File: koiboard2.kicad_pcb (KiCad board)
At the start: 2 copper layers, 227 x 75.4 mm, 137 parts, among them J1 Conn_01x04, J2 USB_C_Receptacle_USB2.0_16P, J3 Conn_01x05, SW1 choc_v1_SW_HS, SW10 choc_v1_SW_HS, SW11 choc_v1_SW_HS, SW12 choc_v1_SW_HS, SW13 choc_v1_SW_HS, SW14 choc_v1_SW_HS, SW15 choc_v1_SW_HS, SW16 choc_v1_SW_HS, SW17 choc_v1_SW_HS, SW18 choc_v1_SW_HS, SW19 choc_v1_SW_HS, SW2 choc_v1_SW_HS, SW20 choc_v1_SW_HS, SW21 choc_v1_SW_HS, SW22 choc_v1_SW_HS, SW23 choc_v1_SW_HS, SW24 choc_v1_SW_HS, SW25 choc_v1_SW_HS, SW26 choc_v1_SW_HS, SW27 choc_v1_SW_HS, SW28 choc_v1_SW_HS, SW29 choc_v1_SW_HS, SW3 choc_v1_SW_HS, SW30 choc_v1_SW_HS, SW31 choc_v1_SW_HS, SW32 choc_v1_SW_HS, SW33 choc_v1_SW_HS, SW34 choc_v1_SW_HS, SW35 choc_v1_SW_HS, SW36 choc_v1_SW_HS, SW37 choc_v1_SW_HS, SW38 choc_v1_SW_HS, SW39 choc_v1_SW_HS, SW4 choc_v1_SW_HS, SW40 choc_v1_SW_HS, SW41 choc_v1_SW_HS, SW42 choc_v1_SW_HS, SW43 choc_v1_SW_HS, SW44 choc_v1_SW_HS, SW45 choc_v1_SW_HS, SW46 choc_v1_SW_HS, SW47 choc_v1_SW_HS, SW5 choc_v1_SW_HS, SW6 choc_v1_SW_HS, SW7 choc_v1_SW_HS, SW8 choc_v1_SW_HS, SW9 choc_v1_SW_HS, U1 XC6206PxxxMR, U2 SRV05-4, U3 RP2040, U4 W25Q128JVS, Y1 Crystal_GND24

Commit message: silkscreen update
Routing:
- net GND: vias 104 -> 106
- net (no net): vias 0 -> 2
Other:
- board text added: "こいぼーど"

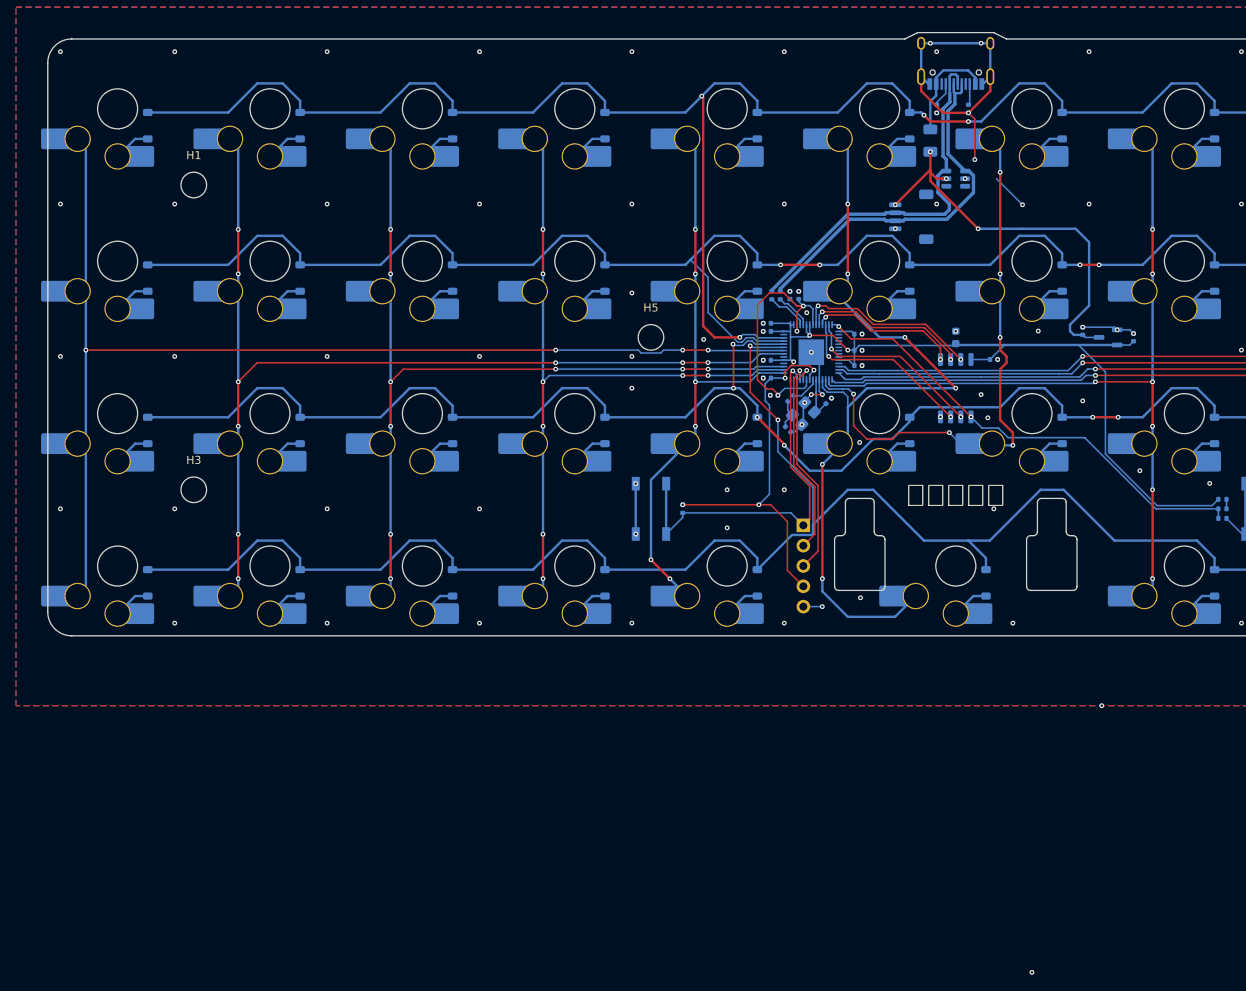
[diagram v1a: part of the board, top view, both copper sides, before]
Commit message: update
new 3d files, stab removed, logo moved, 2x1u <-> 2u support, cleanup, pcb dxf, ect...
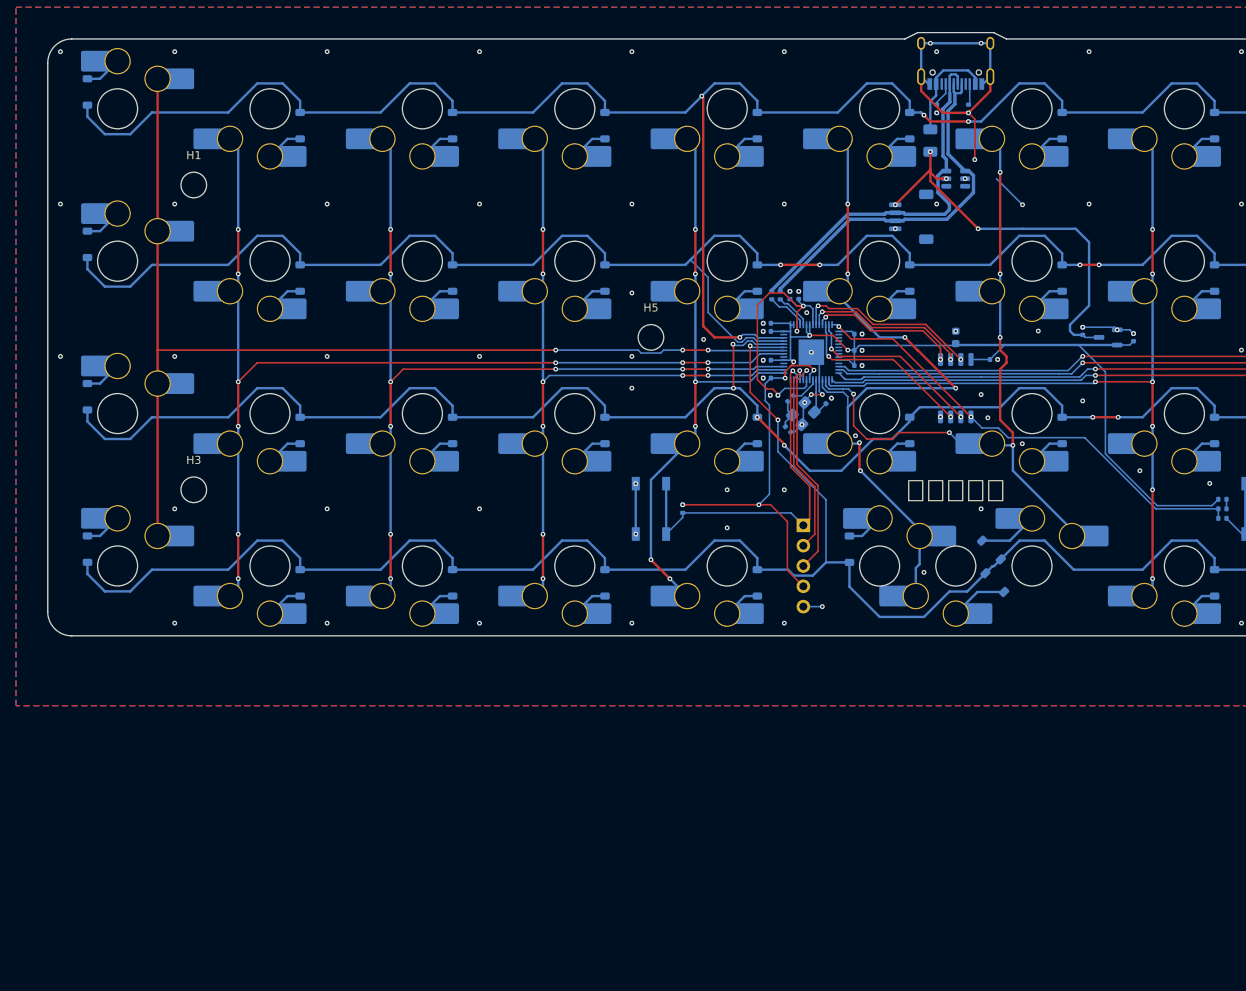
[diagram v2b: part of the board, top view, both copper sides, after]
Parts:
- removed S1: choc_stab, PCM_marbastlib-xp-choc:STAB_choc_2u
- added D43: D_Small, Diode_SMD:D_SOD-123, B.Cu at (138.2, 87.8)
- added D44: D_Small, Diode_SMD:D_SOD-123, B.Cu at (137.8, 83.7)
- added SW43: choc_v1_SW_HS, PCM_marbastlib-xp-choc:SW_choc_v2_HS_CPG135001S30_1u, B.Cu at (133.3, 85.7)
- added SW44: choc_v1_SW_HS, Cool Library:SW_choc_v2_HS_CPG135001S30_1u_switch_hide, B.Cu at (142.9, 85.7)
- J3: footprint Connector_PinHeader_2.54mm:PinHeader_1x05_P2.54mm_Vertical -> Cool Library:PinHeader_1x05_P2.54mm_Vertical_No_3D_Header
- SW42: footprint PCM_marbastlib-xp-choc:SW_choc_v2_HS_CPG135001S30_1u -> Cool Library:SW_choc_v2_HS_CPG135001S30_1u_switch_hide
- moved D42 17.6 mm to (120.1, 83.6), turned to 90 degrees
- moved SW42 9.52 mm to (123.8, 85.7), turned to 0 degrees
- moved D37 8.64 mm to (24.8, 83.6), turned to 90 degrees
- moved D25 8.64 mm to (24.8, 64.6), turned to 90 degrees
- moved D13 8.64 mm to (24.8, 45.5), turned to 90 degrees
- moved D1 8.64 mm to (24.8, 26.5), turned to 90 degrees
- turned SW37 to 0 degrees
- turned SW25 to 0 degrees
- turned SW13 to 0 degrees
- turned SW1 to 0 degrees
- renumbered C16 to C10, C8 to C11, C9 to C12, C10 to C14, C11 to C15, C12 to C16, C14 to C8, C15 to C9, D43 to D45, D44 to D46, D45 to D47, D46 to D48, D47 to D49, SW43 to SW45, SW44 to SW46, SW45 to SW47, SW46 to SW48, SW47 to SW49
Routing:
- net COL6: track 71.1 -> 85.5 mm
- net ROW3: track 290.0 -> 301.6 mm
- net COL0: track 147.3 -> 135.7 mm, vias 4 -> 3
- net ROW0: track 292.7 -> 303.7 mm
- net ROW2: track 266.4 -> 277.4 mm
- net ROW1: track 270.8 -> 281.8 mm
- net COL5: track 98.7 -> 90.3 mm
- net Net-(D44-A): track 0.00 -> 7.39 mm
- net Net-(D43-A): track 0.00 -> 7.16 mm
- net GND: vias 106 -> 105
- net (no net): vias 2 -> 0
